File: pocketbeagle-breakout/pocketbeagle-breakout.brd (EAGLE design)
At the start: 102.9 x 68.6 mm, 91 parts, among them J30 4-1734592-04-1734592-0, J31 4-1734592-04-1734592-0, J5 POWER_JACKSLT, P1 BCS-118-L-D-TE, P1IN BCS-118-L-D-TE, P2 BCS-118-L-D-TE, P2IN BCS-118-L-D-TE, U1 TCAN330

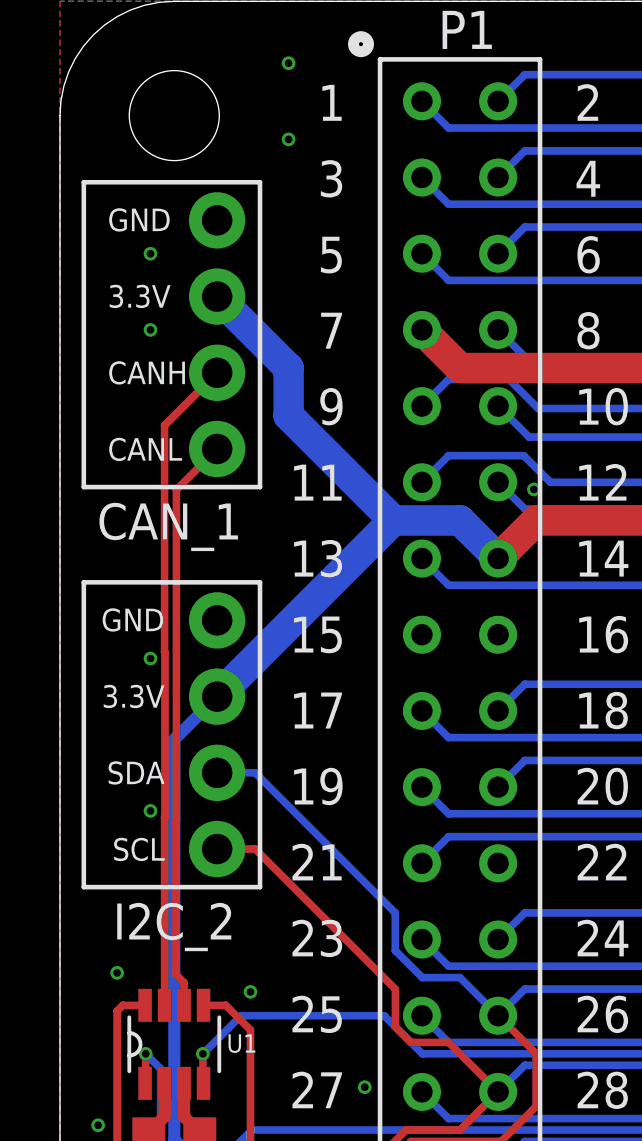
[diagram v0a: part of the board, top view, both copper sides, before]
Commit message: slightly moved connector
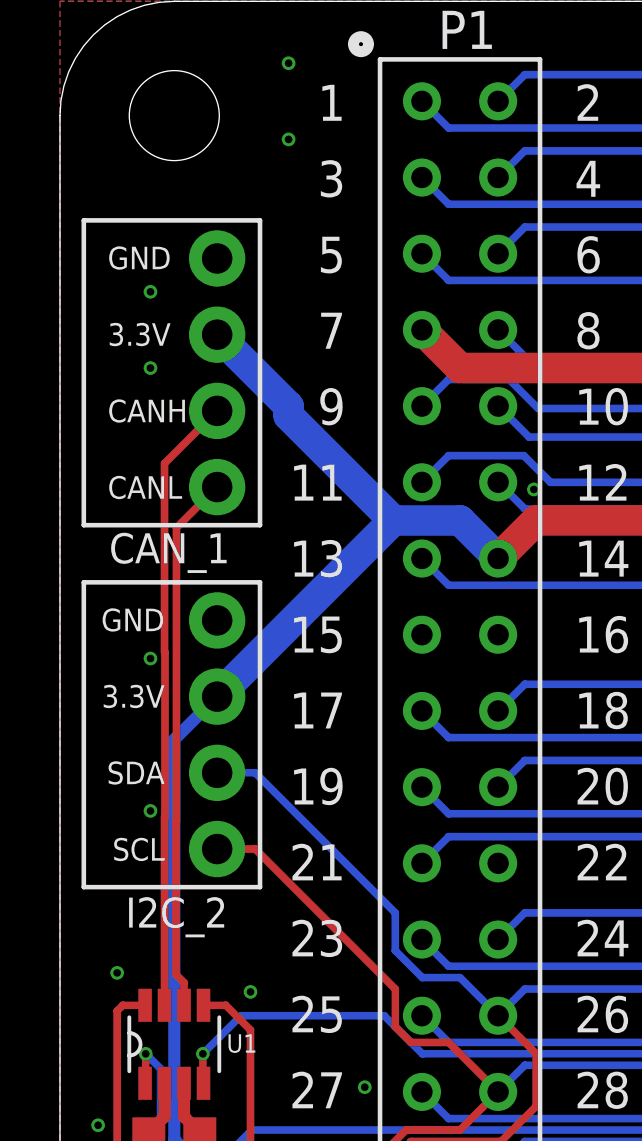
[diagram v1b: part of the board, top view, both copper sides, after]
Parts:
- moved J29 1.27 mm to (5.24, 60.0)
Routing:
- net CAN_L: track 19.2 -> 18.0 mm
- net 3.3V: track 145.6 -> 144.3 mm
- net CAN_H: track 21.8 -> 20.6 mm
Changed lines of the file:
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@@
 SDA
 SCL</text>
-<text x="3.65125" y="50.64125" size="1.2" layer="21" font="vector" ratio="10" distance="111" align="bottom-center">CAN_1</text>
-<text x="3.81" y="37.30625" size="1.2" layer="21" font="vector" ratio="10" distance="111" align="bottom-center">I2C_2</text>
-<text x="1.5875" y="61.66875" size="0.75" layer="21" font="vector" ratio="10" distance="240" align="top-left">GND
+<text x="3.65125" y="49.8475" size="1" layer="21" font="vector" ratio="10" distance="111" align="bottom-center">CAN_1</text>
+<text x="3.889375" y="37.703125" size="1" layer="21" font="vector" ratio="10" distance="111" align="bottom-center">I2C_2</text>
+<text x="1.5875" y="60.39875" size="0.75" layer="21" font="vector" ratio="10" distance="240" align="top-left">GND
 3.3V
 CANH
@@
 MAX</text>
 <wire x1="0.79375" y1="39.0525" x2="0.79375" y2="49.2125" width="0.1524" layer="21"/>
-<wire x1="6.6675" y1="62.5475" x2="6.6675" y2="52.3875" width="0.1524" layer="21"/>
-<wire x1="6.6675" y1="52.3875" x2="0.79375" y2="52.3875" width="0.1524" layer="21"/>
-<wire x1="0.79375" y1="62.5475" x2="6.6675" y2="62.5475" width="0.1524" layer="21"/>
-<wire x1="0.79375" y1="52.3875" x2="0.79375" y2="62.5475" width="0.1524" layer="21"/>
+<wire x1="6.6675" y1="61.2775" x2="6.6675" y2="51.1175" width="0.1524" layer="21"/>
+<wire x1="6.6675" y1="51.1175" x2="0.79375" y2="51.1175" width="0.1524" layer="21"/>
+<wire x1="0.79375" y1="61.2775" x2="6.6675" y2="61.2775" width="0.1524" layer="21"/>
+<wire x1="0.79375" y1="51.1175" x2="0.79375" y2="61.2775" width="0.1524" layer="21"/>
 <text x="77.55485" y="21.351825" size="0.75" layer="21" font="vector" ratio="10" distance="240" rot="R90">GND
 CLK2
@@
 <attribute name="PROD_ID" value="CAP-08390" x="93.10688125" y="49.371246875" size="1.778" layer="27" rot="R270" display="off"/>
 </element>
-<element name="J29" library="SparkFun-Connectors" package="1X04_NO_SILK" package3d_urn="urn:adsk.eagle:package:38094/1" value="" x="5.23875" y="61.2775" smashed="yes" rot="R270">
-<attribute name="PROD_ID" value="CONN-09696" x="5.23875" y="61.2775" size="1.778" layer="27" rot="R270" display="off"/>
-<attribute name="VALUE" x="2.57175" y="62.5475" size="0.6096" layer="27" font="vector" ratio="20" rot="R270"/>
+<element name="J29" library="SparkFun-Connectors" package="1X04_NO_SILK" package3d_urn="urn:adsk.eagle:package:38094/1" value="" x="5.23875" y="60.0075" smashed="yes" rot="R270">
+<attribute name="PROD_ID" value="CONN-09696" x="5.23875" y="60.0075" size="1.778" layer="27" rot="R270" display="off"/>
+<attribute name="VALUE" x="2.57175" y="61.2775" size="0.6096" layer="27" font="vector" ratio="20" rot="R270"/>
 </element>
 <element name="SJ1" library="SparkFun-Passives" package="SJ_2S-NOTRACE" value="SOLDERJUMPERNC2" x="23.1775" y="18.57375" smashed="yes" rot="MR270">
@@
 <via x="3.01625" y="41.5925" extent="1-16" drill="0.254"/>
 <via x="3.01625" y="46.6725" extent="1-16" drill="0.254"/>
-<via x="3.01625" y="57.62625" extent="1-16" drill="0.254"/>
-<via x="3.01625" y="60.16625" extent="1-16" drill="0.254"/>
+<via x="3.01625" y="56.35625" extent="1-16" drill="0.254"/>
+<via x="3.01625" y="58.89625" extent="1-16" drill="0.254"/>
 <via x="7.62" y="63.97625" extent="1-16" drill="0.254"/>
 <via x="7.62" y="66.51625" extent="1-16" drill="0.254"/>
@@
 <wire x1="11.1125" y1="51.27625" x2="13.335" y2="51.27625" width="1.016" layer="16"/>
 <wire x1="11.1125" y1="51.27625" x2="7.62" y2="54.76875" width="1.016" layer="16"/>
-<wire x1="7.62" y1="54.76875" x2="7.62" y2="56.35625" width="1.016" layer="16"/>
-<wire x1="7.62" y1="56.35625" x2="5.23875" y2="58.7375" width="1.016" layer="16"/>
+<wire x1="7.62" y1="54.76875" x2="7.62" y2="55.08625" width="1.016" layer="16"/>
+<wire x1="7.62" y1="55.08625" x2="5.23875" y2="57.4675" width="1.016" layer="16"/>
 <wire x1="48.895" y1="37.30625" x2="50.165" y2="36.03625" width="1.016" layer="16"/>
 <wire x1="59.055" y1="36.03625" x2="60.325" y2="37.30625" width="1.016" layer="16"/>
@@
 <contactref element="J29" pad="3"/>
 <contactref element="U1" pad="7"/>
-<wire x1="3.485" y1="54.44375" x2="5.23875" y2="56.1975" width="0.254" layer="1"/>
+<wire x1="3.485" y1="53.17375" x2="5.23875" y2="54.9275" width="0.254" layer="1"/>
 <wire x1="3.485" y1="35.11375" x2="3.485" y2="41.37875" width="0.254" layer="1"/>
 <wire x1="3.485" y1="41.37875" x2="3.49885" y2="41.3926" width="0.254" layer="1"/>
 <wire x1="3.49885" y1="46.8724" x2="3.485" y2="46.88625" width="0.254" layer="1"/>
-<wire x1="3.485" y1="46.88625" x2="3.485" y2="54.44375" width="0.254" layer="1"/>
+<wire x1="3.485" y1="46.88625" x2="3.485" y2="53.17375" width="0.254" layer="1"/>
 <wire x1="3.49885" y1="41.3926" x2="3.49885" y2="46.8724" width="0.254" layer="1"/>
 </signal>
@@
 <wire x1="3.866" y1="41.22093125" x2="3.87985" y2="41.23478125" width="0.254" layer="1"/>
 <wire x1="3.866" y1="36.139" x2="3.866" y2="41.22093125" width="0.254" layer="1"/>
-<wire x1="3.87985" y1="52.2986" x2="5.23875" y2="53.6575" width="0.254" layer="1"/>
-<wire x1="3.87985" y1="41.23478125" x2="3.87985" y2="52.2986" width="0.254" layer="1"/>
+<wire x1="3.87985" y1="41.23478125" x2="3.879853125" y2="51.028603125" width="0.254" layer="1"/>
+<wire x1="3.879853125" y1="51.028603125" x2="5.23875" y2="52.3875" width="0.254" layer="1"/>
 </signal>
 <signal name="N$20">
